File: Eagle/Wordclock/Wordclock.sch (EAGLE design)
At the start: 266 parts, among them IC1 MEGA8-P, Q3 SUP75N06-08

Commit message: layout der leds
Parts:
- added PAD3, PAD4: (no value), wirepad:2,54/1,1
- R1, R2: device rcl:R-EU_M0805 -> rcl:R-EU_R1206
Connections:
- net GND: now also PAD4.P
- net VDD: now also PAD3.P
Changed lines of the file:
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@@
 <part name="GND220" library="supply1" deviceset="GND" device=""/>
 <part name="GND221" library="supply1" deviceset="GND" device=""/>
-<part name="R1" library="rcl" deviceset="R-EU_" device="M0805"/>
-<part name="R2" library="rcl" deviceset="R-EU_" device="M0805"/>
+<part name="R1" library="rcl" deviceset="R-EU_" device="R1206"/>
+<part name="R2" library="rcl" deviceset="R-EU_" device="R1206"/>
 <part name="R_LED1" library="rcl" deviceset="R-EU_" device="M1206"/>
 <part name="R_LED2" library="rcl" deviceset="R-EU_" device="M1206"/>
@@
 <part name="R_LED5" library="rcl" deviceset="R-EU_" device="M1206"/>
 <part name="P+11" library="supply1" deviceset="+5V" device=""/>
+<part name="PAD3" library="wirepad" deviceset="2,54/1,1" device=""/>
+<part name="PAD4" library="wirepad" deviceset="2,54/1,1" device=""/>
 </parts>
 <sheets>
@@
 <instance part="R_LED5" gate="G$1" x="-76.2" y="22.86" rot="R90"/>
 <instance part="P+11" gate="1" x="-76.2" y="33.02"/>
+<instance part="PAD3" gate="1" x="-7.62" y="-50.8" rot="R180"/>
+<instance part="PAD4" gate="1" x="-7.62" y="-58.42" rot="R180"/>
 </instances>
 <busses>
@@
 <pinref part="GND231" gate="1" pin="GND"/>
 <wire x1="-101.6" y1="-25.4" x2="-101.6" y2="-45.72" width="0.1524" layer="91"/>
+</segment>
+<segment>
+<pinref part="PAD4" gate="1" pin="P"/>
+<wire x1="-12.7" y1="-58.42" x2="-10.16" y2="-58.42" width="0.1524" layer="91"/>
+<label x="-12.7" y="-58.42" size="1.778" layer="95" rot="R180" xref="yes"/>
 </segment>
 </net>
@@
 <label x="33.02" y="10.16" size="1.778" layer="95" rot="R270" xref="yes"/>
 </segment>
+<segment>
+<pinref part="PAD3" gate="1" pin="P"/>
+<wire x1="-12.7" y1="-50.8" x2="-10.16" y2="-50.8" width="0.1524" layer="91"/>
+<label x="-12.7" y="-50.8" size="1.778" layer="95" rot="R180" xref="yes"/>
+</segment>
 </net>

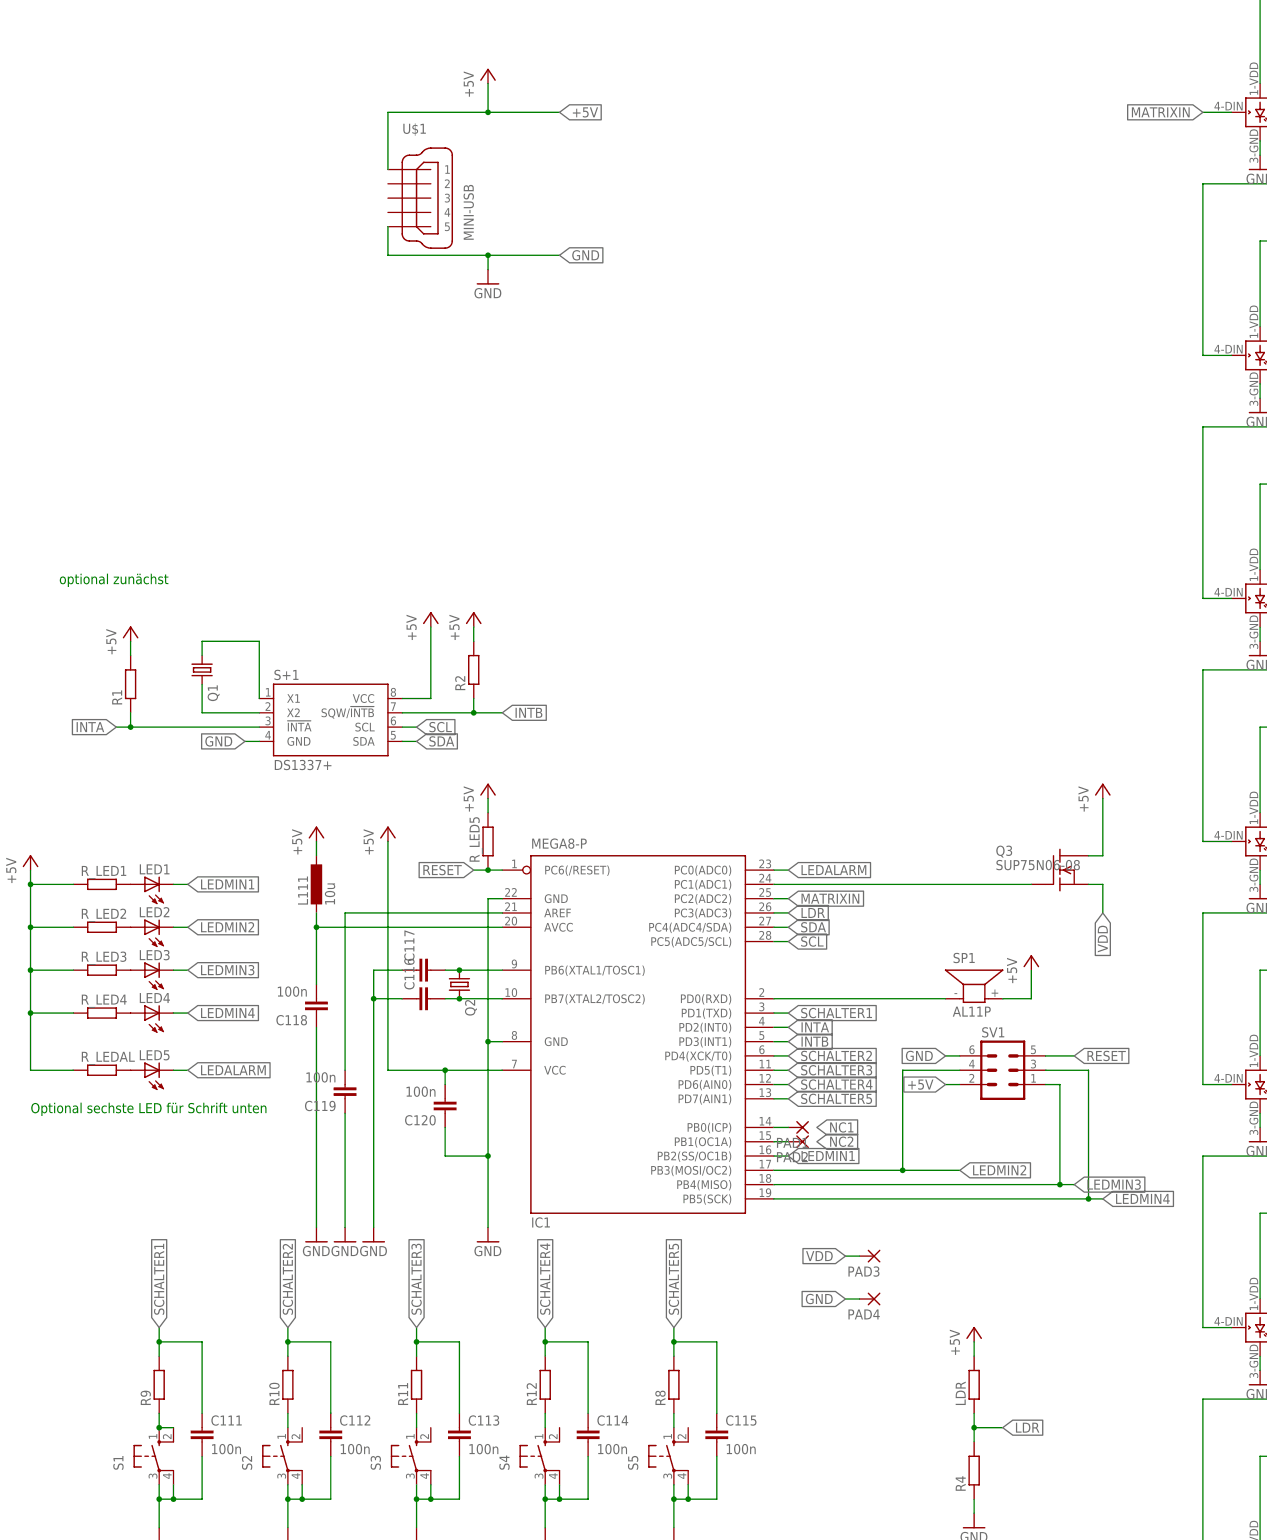
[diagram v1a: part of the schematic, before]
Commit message: Eagle untere hälfte der Platine und LED Layout fertig
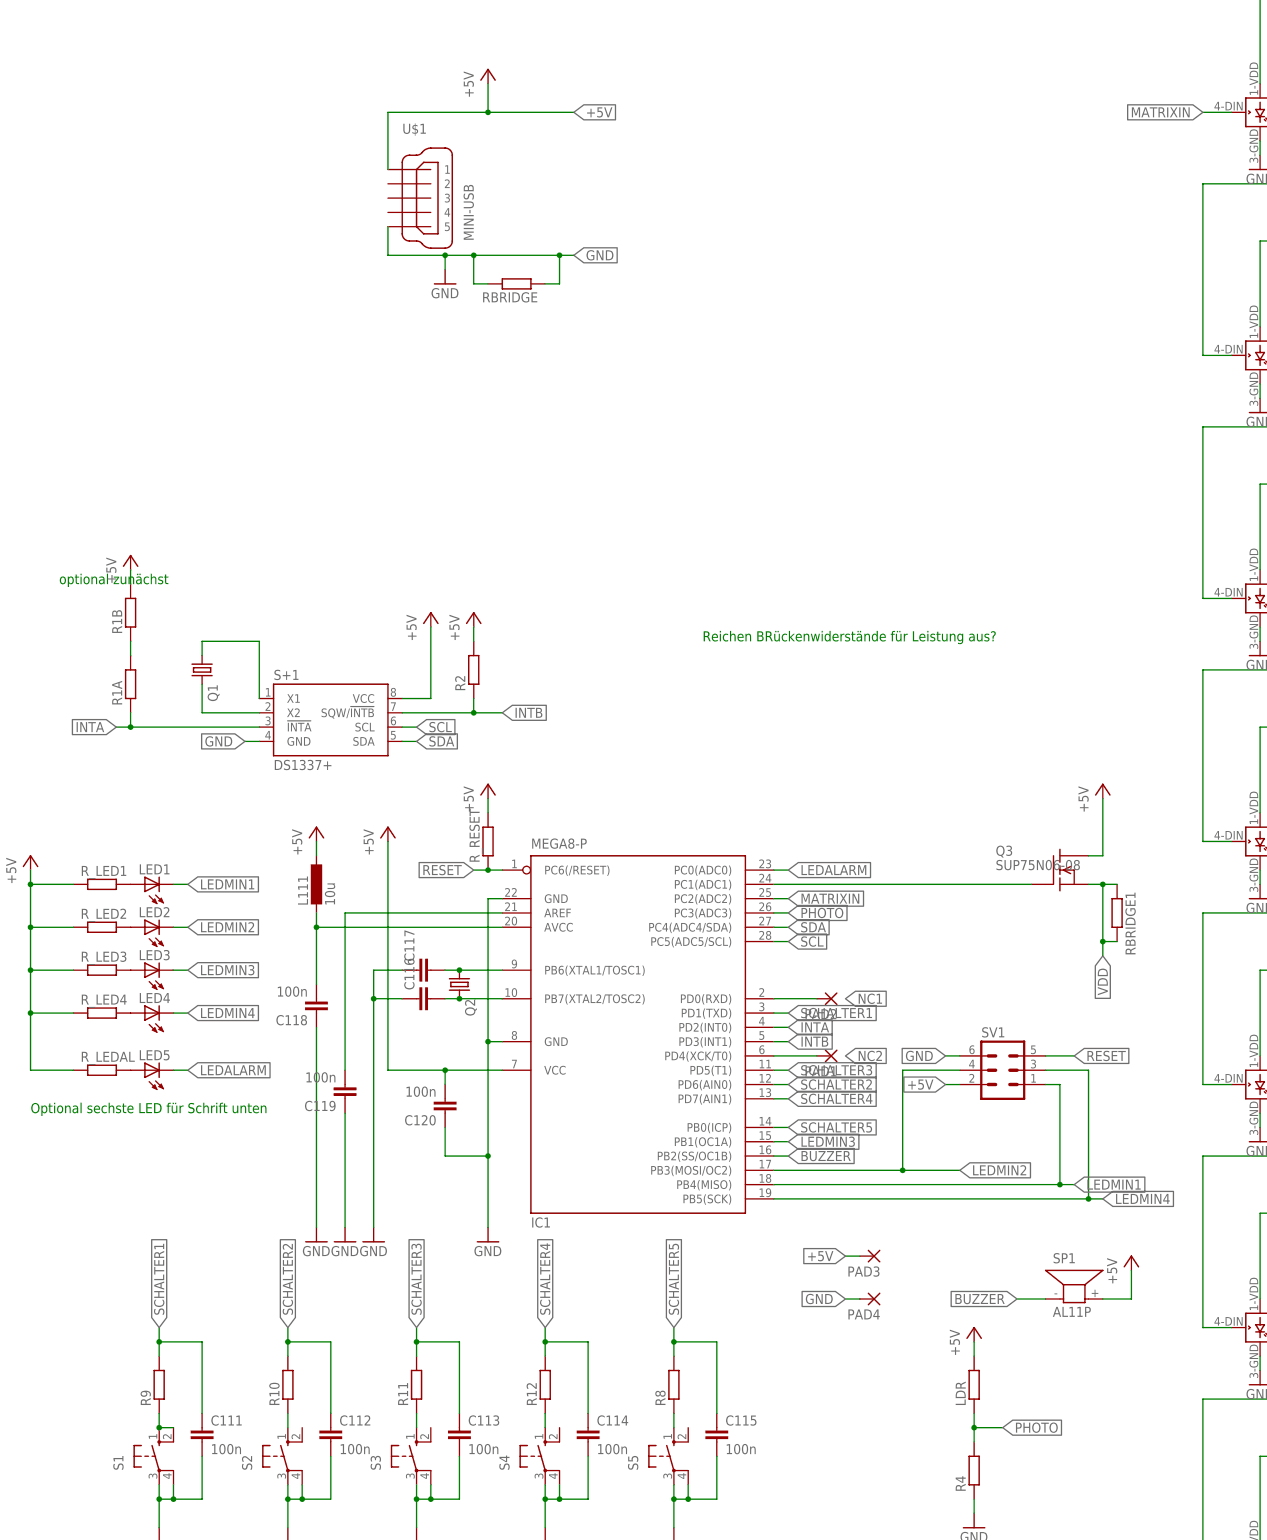
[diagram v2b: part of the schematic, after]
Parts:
- added R1B, RBRIDGE, RBRIDGE1: (no value), rcl:R-EU_R1206
- C111, C112, C113, C114, C115: device rcl:C-EUC1310 -> rcl:C-EUC1206
- LDR: device rcl:R-EU_M1206 -> rcl:R-EU_0204/5
- renumbered R1 to R1A, R_LED5 to R_RESET
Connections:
- net LDR renamed PHOTO
- net N$127 renamed MOSFET
- removed net N$112: IC1.PD0(RXD), SP1.1
- new net BUZZER: IC1.PB2(SS/OC1B), SP1.1
- new net N$124: R1A.2, R1B.1
- net +5V: now also PAD3.P, R1B.2; no longer R1A.2
- net GND: now also RBRIDGE.1, RBRIDGE.2
- net LEDMIN1: now also IC1.PB4(MISO), SV1.1; no longer IC1.PB2(SS/OC1B)
- net LEDMIN3: now also IC1.PB1(OC1A); no longer IC1.PB4(MISO), SV1.1
- net NC1: now also IC1.PD0(RXD), PAD2.P; no longer IC1.PB0(ICP), PAD1.P
- net NC2: now also IC1.PD4(XCK/T0), PAD1.P; no longer IC1.PB1(OC1A), PAD2.P
- net SCHALTER2: now also IC1.PD6(AIN0); no longer IC1.PD4(XCK/T0)
- net SCHALTER4: now also IC1.PD7(AIN1); no longer IC1.PD6(AIN0)
- net SCHALTER5: now also IC1.PB0(ICP); no longer IC1.PD7(AIN1)
- net VDD: now also RBRIDGE1.1, RBRIDGE1.2; no longer PAD3.P
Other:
- note added: "Reichen BRückenwiderstände für Leistung aus?"
- moved on the sheet: PAD1, PAD2, SP1

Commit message: Layout fertig
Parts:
- removed R1B: (no value), rcl:R-EU_R1206
- added BRIDGE_RESET: (no value), rcl:R-EU_M1206
- added R6, R7, RBRIDGE2, RBRIDGE3, RBRIDGE4, RBRIDGE5, R_MOSFET: (no value), rcl:R-EU_R1206
- C118: device rcl:C-EUC0805 -> rcl:C-EUC1206
- renumbered R1A to R1
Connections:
- removed net MOSFET: IC1.PC1(ADC1), Q3.G
- new net INTB_UNBRIDGED: R2.1, RBRIDGE3.2, S+1.SQW/!INTB!
- new net MOSFET_A: IC1.PC1(ADC1), R_MOSFET.1
- new net MOSFET_B: Q3.G, R_MOSFET.2
- new net N$112: R6.2, S+1.SCL
- new net N$125: BRIDGE_RESET.1, IC1.PC6(/RESET), R_RESET.1
- new net N$127: RBRIDGE2.1, SV1.4
- new net N$128: RBRIDGE4.1, SV1.3
- new net N$129: RBRIDGE5.1, SV1.5
- net +5V: now also R1.2; no longer R1B.2
- net INTA: now also IC1.PD3(INT1); no longer IC1.PD2(INT0)
- net INTB: now also IC1.PD2(INT0), RBRIDGE3.1; no longer IC1.PD3(INT1), R2.1, S+1.SQW/!INTB!
- net LEDALARM: now also IC1.PC3(ADC3); no longer IC1.PC0(ADC0)
- net LEDMIN2: now also RBRIDGE2.2; no longer SV1.4
- net LEDMIN4: now also RBRIDGE4.2; no longer SV1.3
- net MATRIXIN: now also IC1.PD0(RXD); no longer IC1.PC2(ADC2)
- net N$124: now also R7.2, S+1.SDA; no longer R1.2, R1B.1
- net NC1: now also IC1.PC0(ADC0); no longer IC1.PD0(RXD)
- net PHOTO: now also IC1.PC2(ADC2); no longer IC1.PC3(ADC3)
- net RESET: now also BRIDGE_RESET.2, RBRIDGE5.2; no longer IC1.PC6(/RESET), R_RESET.1, SV1.5
- net SCL: now also R6.1; no longer S+1.SCL
- net SDA: now also R7.1; no longer S+1.SDA
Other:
- moved on the sheet: PAD2, R_RESET

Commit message: Schutzwiderstand für WS2812 added
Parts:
- removed BRIDGE_RESET, R10, R11, R12, R4, R8, R9: (no value), rcl:R-EU_M1206
- removed C111, C112, C113, C114, C115: 100n, rcl:C-EUC1206
- removed LED5: (no value), led:LEDCHIPLED_1206
- removed Q1: (no value), crystal:CRYSTALHC49S
- removed R1, R2, R6, R7, RBRIDGE, RBRIDGE1, RBRIDGE2, RBRIDGE3, RBRIDGE4, RBRIDGE5: (no value), rcl:R-EU_R1206
- added BRIDGE_GND: 0, rcl:R-EU_R1206
- added BRIDGE_INTB, BRIDGE_MOSI, BRIDGE_RESET2, BRIDGE_SCK, BRIDGE_VDD, PULLUP_INTA, PULLUP_INTB, R_MATRIXIN, R_SCL, R_SDA: (no value), rcl:R-EU_R1206
- added BRIDGE_RESET1: 0, rcl:R-EU_M1206
- added C_S1, C_S2, C_S3, C_S4, C_S5: 100n, rcl:C-EUC1206
- added LEDAL: (no value), led:LEDCHIPLED_1206
- added Q_DS: (no value), crystal:CRYSTALHC49S
- added R_PHOTO, R_S1, R_S2, R_S3, R_S4, R_S5: (no value), rcl:R-EU_M1206
- R_RESET: value (none) -> 10k
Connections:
- new net N$130: L1.DIN, R_MATRIXIN.2
- net +5V: now also PULLUP_INTA.2, PULLUP_INTB.2; no longer R1.2, R2.2
- net GND: now also BRIDGE_GND.1, BRIDGE_GND.2, C_S1.2, C_S2.2, C_S3.2, C_S4.2, C_S5.2, R_PHOTO.1; no longer C111.2, C112.2, C113.2, C114.2, C115.2, R4.1, RBRIDGE.1, RBRIDGE.2
- net INTA: now also PULLUP_INTA.1; no longer R1.1
- net INTB: now also BRIDGE_INTB.1; no longer RBRIDGE3.1
- net INTB_UNBRIDGED: now also BRIDGE_INTB.2, PULLUP_INTB.1; no longer R2.1, RBRIDGE3.2
- net LEDALARM: now also LEDAL.C; no longer LED5.C
- net LEDMIN2: now also BRIDGE_MOSI.2; no longer RBRIDGE2.2
- net LEDMIN4: now also BRIDGE_SCK.2; no longer RBRIDGE4.2
- net MATRIXIN: now also R_MATRIXIN.1; no longer L1.DIN
- net N$112: now also R_SCL.2; no longer R6.2
- net N$118: now also LEDAL.A; no longer LED5.A
- net N$119: now also R_S1.1; no longer R9.1
- net N$120: now also R_S2.1; no longer R10.1
- net N$121: now also R_S3.1; no longer R11.1
- net N$122: now also R_S4.1; no longer R12.1
- net N$124: now also R_SDA.2; no longer R7.2
- net N$125: now also BRIDGE_RESET1.1; no longer BRIDGE_RESET.1
- net N$126: now also R_S5.1; no longer R8.1
- net N$127: now also BRIDGE_MOSI.1; no longer RBRIDGE2.1
- net N$128: now also BRIDGE_SCK.1; no longer RBRIDGE4.1
- net N$129: now also BRIDGE_RESET2.1; no longer RBRIDGE5.1
- net N$20: now also Q_DS.1; no longer Q1.1
- net N$21: now also Q_DS.2; no longer Q1.2
- net PHOTO: now also R_PHOTO.2; no longer R4.2
- net RESET: now also BRIDGE_RESET1.2, BRIDGE_RESET2.2; no longer BRIDGE_RESET.2, RBRIDGE5.2
- net SCHALTER1: now also C_S1.1, R_S1.2; no longer C111.1, R9.2
- net SCHALTER2: now also C_S2.1, R_S2.2; no longer C112.1, R10.2
- net SCHALTER3: now also C_S3.1, R_S3.2; no longer C113.1, R11.2
- net SCHALTER4: now also C_S4.1, R_S4.2; no longer C114.1, R12.2
- net SCHALTER5: now also C_S5.1, R_S5.2; no longer C115.1, R8.2
- net SCL: now also R_SCL.1; no longer R6.1
- net SDA: now also R_SDA.1; no longer R7.1
- net VDD: now also BRIDGE_VDD.1, BRIDGE_VDD.2; no longer RBRIDGE1.1, RBRIDGE1.2
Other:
- note added: "Pads für Vesorgung späterer Schaltungsteile z.B. Bewegungsmelder"
- note removed: "Optional sechste LED für Schrift unten"
- moved on the sheet: C116, C117, C118, C119, C120, IC1, L111, LDR, LED1, LED2, LED3, LED4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

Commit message: SCL/SDA Pullups hinzugefügt
ACHTUNG!!! Diese Pullups sind auf der ersten Platine noch nicht
enthalten
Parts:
- added PULLUP_SCL, PULLUP_SDA: 4,7k, rcl:R-EU_R1206
- BRIDGE_INTB, BRIDGE_MOSI, BRIDGE_RESET2, BRIDGE_SCK, BRIDGE_VDD: value (none) -> 0
- C116, C117: value (none) -> 18p
- PULLUP_INTA, PULLUP_INTB: value (none) -> 4,7k
- Q_DS: value (none) -> 32,768MHz
- R_MATRIXIN: value (none) -> 300
- R_MOSFET: value (none) -> 130
- R_S1, R_S2, R_S3, R_S4, R_S5: value (none) -> 1k
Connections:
- net +5V: now also PULLUP_SCL.2, PULLUP_SDA.2
- net N$112: now also PULLUP_SCL.1
- net N$124: now also PULLUP_SDA.1
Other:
- moved on the sheet: BRIDGE_INTB, BRIDGE_RESET2, R_SCL, R_SDA

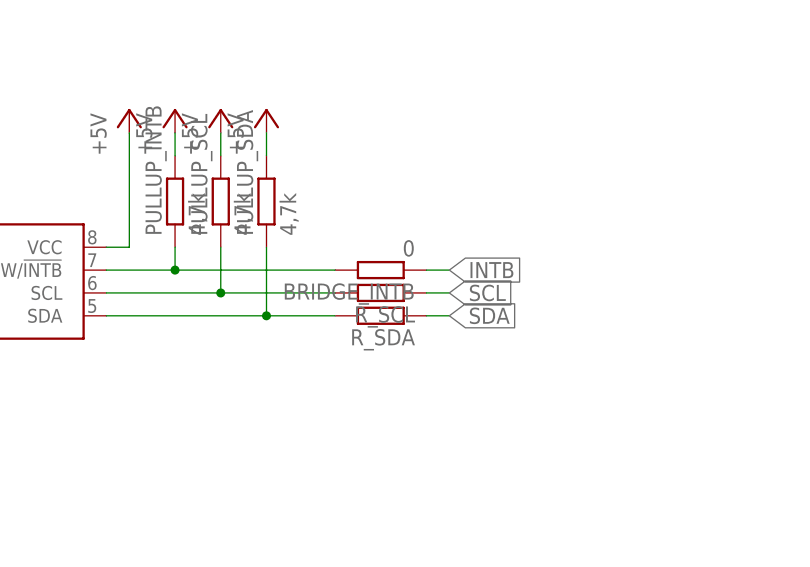
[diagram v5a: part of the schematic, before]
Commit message: weiter Bauteilewerte angepasst
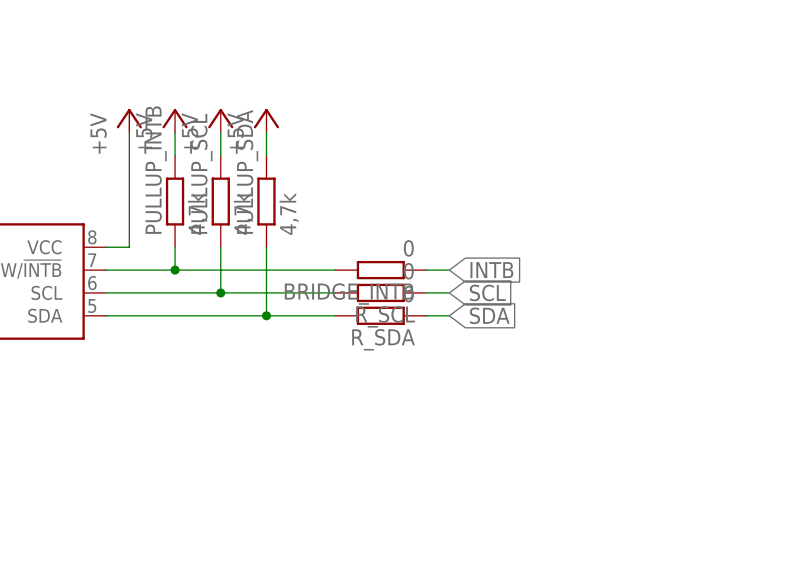
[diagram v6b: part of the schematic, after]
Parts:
- R_SCL, R_SDA: value (none) -> 0
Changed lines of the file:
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@@
 <part name="BRIDGE_INTB" library="rcl" deviceset="R-EU_" device="R1206" value="0"/>
 <part name="R_MOSFET" library="rcl" deviceset="R-EU_" device="R1206" value="130"/>
-<part name="R_SCL" library="rcl" deviceset="R-EU_" device="R1206"/>
-<part name="R_SDA" library="rcl" deviceset="R-EU_" device="R1206"/>
+<part name="R_SCL" library="rcl" deviceset="R-EU_" device="R1206" value="0"/>
+<part name="R_SDA" library="rcl" deviceset="R-EU_" device="R1206" value="0"/>
 <part name="BRIDGE_RESET1" library="rcl" deviceset="R-EU_" device="M1206" value="0"/>
 <part name="BRIDGE_MOSI" library="rcl" deviceset="R-EU_" device="R1206" value="0"/>
